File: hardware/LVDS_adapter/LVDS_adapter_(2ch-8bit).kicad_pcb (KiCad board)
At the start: 2 copper layers, 27 x 31.1 mm, 17 parts, among them J1 DF12NB(3.0)-30DS-0.5V(51), J2 Conn_02x15_Odd_Even, J3 Conn_01x06_Socket, J4 DF12NB(3.0)-30DS-0.5V(51), J5 Conn_01x06_Socket, J6 Conn_01x02

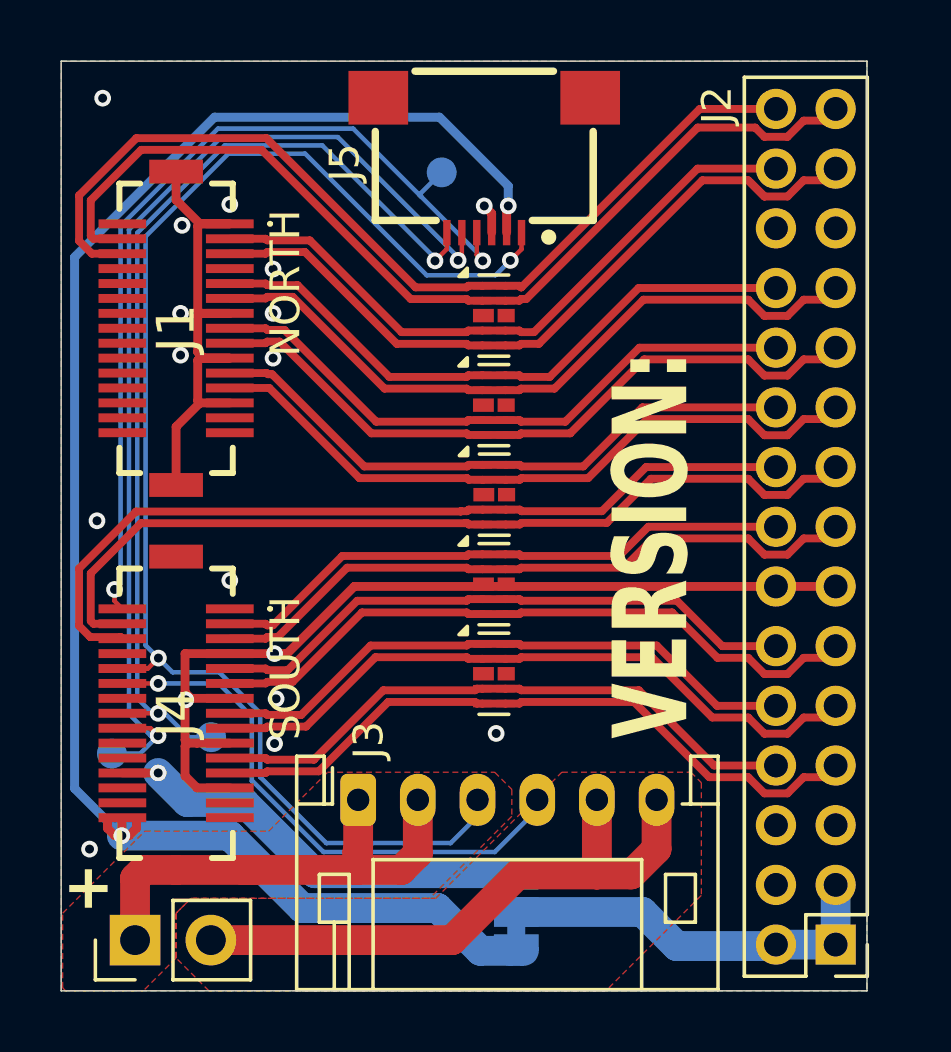
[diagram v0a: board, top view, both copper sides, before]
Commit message: change 2x15 vertical header for an edge one
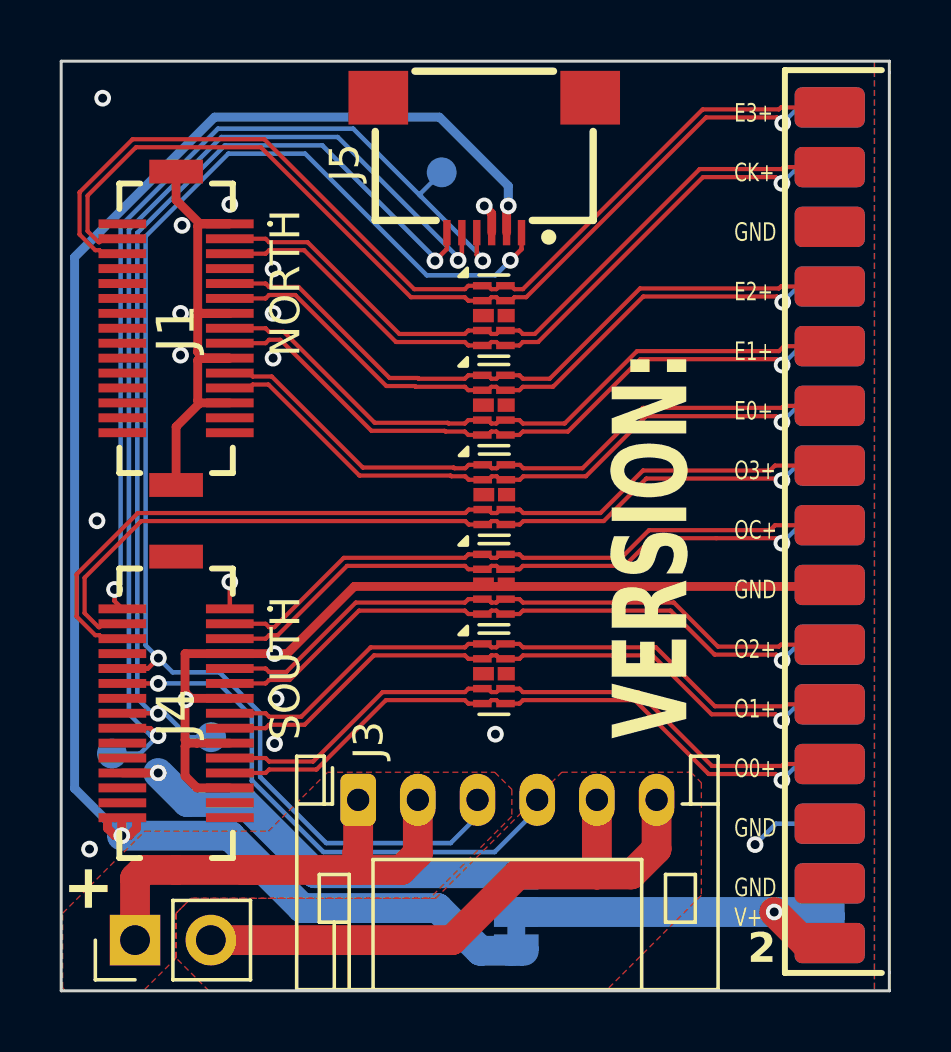
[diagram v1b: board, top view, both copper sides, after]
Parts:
- moved J2 29.1 mm to (152.5, 74.8), turned to 0 degrees
- moved G*** 2.57 mm to (143.8, 85.5)
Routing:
- net GND: track 50.7 -> 54.4 mm, vias 17 -> 18
- net LVDS_OC_P: track 19.7 -> 21.9 mm
- net LVDS_E1_P: track 20.7 -> 22.7 mm
- net LVDS_E0_P: track 20.5 -> 22.5 mm
- net LVDS_EC_P: track 21.9 -> 23.9 mm
- net LVDS_E2_P: track 20.9 -> 22.9 mm
- net LVDS_O0_P: track 20.4 -> 22.4 mm
- net LVDS_O1_P: track 20.2 -> 22.1 mm
- net LVDS_O2_P: track 20.0 -> 21.9 mm
- net LVDS_E3_P: track 31.9 -> 33.8 mm
- net LVDS_O3_P: track 28.4 -> 30.2 mm
- net Net-(J2-Pin_1): track 13.2 -> 14.8 mm, vias 0 -> 1
- net LVDS_EC_N: track 25.2 -> 24.2 mm, vias 0 -> 1
- net LVDS_O2_N: track 22.6 -> 22.2 mm, vias 0 -> 1
- net LVDS_O1_N: track 22.8 -> 22.4 mm, vias 0 -> 1
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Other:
- board size 27 x 31.1 mm -> 27.8 x 31.1 mm
- board text added: "2 layer JLC0212 1.2mm, 1oz coplanar 100 ohm differential .1420mm separation .127mm (JLCPCB calculator)"
- board text added: "E3+ CK+ GND E2+ E1+ E0+ O3+ OC+ GND O2+ O1+ O0+ GND GND V+"
- board text added: "E3- CK- GND E2- E1- E0- O3- OC- GND O2- O1- O0- GND V+ V+"
- board text removed: "E3-+ CK-+ G/G E2-+ E1-+ E0-+ O3-+ OC-+ G/G O2-+ O1-+ O0-+ G/G V+/G V+V+"

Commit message: review and update manufacturing constraints (via size, etc.)
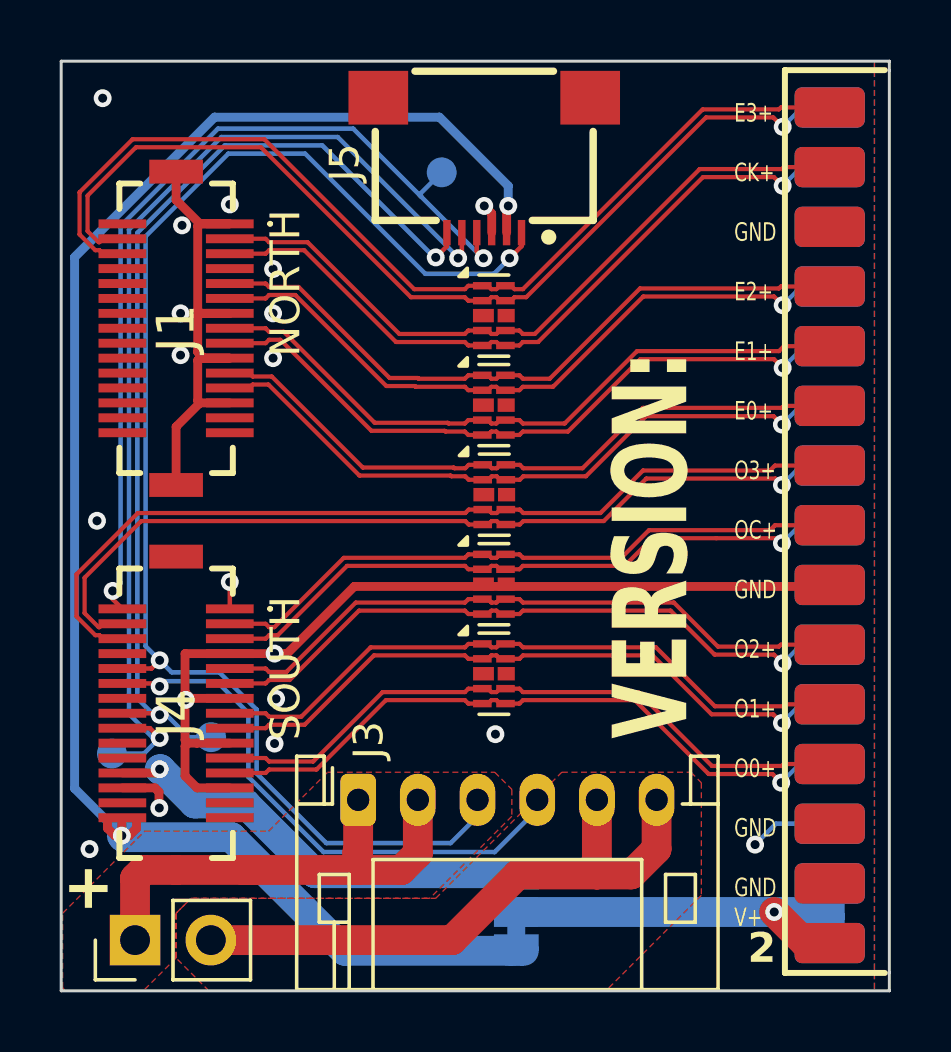
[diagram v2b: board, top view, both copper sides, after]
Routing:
- net GND: track 54.4 -> 56.2 mm, vias 18 -> 19
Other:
- outline, holes or cut-outs redrawn
